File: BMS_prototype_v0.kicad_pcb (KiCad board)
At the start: 2 copper layers, 117 parts, among them J1 Conn_02x12_Odd_Even, J2 Conn_01x13_Pin, J3 Conn_01x02_Pin, J4 Conn_01x02_Pin, J5 Conn_02x08_Odd_Even, J7 Conn_01x03_Pin, Q2 Q_NMOS_GSD, Q3 Q_NMOS_GSD, Q4 Q_NMOS_GSD, Q5 Q_NMOS_GSD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

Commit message: add Res Shunt e atualiza para Kicad 9.0
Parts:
- removed NT1: NetTie_2, NetTie:NetTie-2_SMD_Pad0.5mm
- added SW1: SW_DIP_x01, Button_Switch_THT:SW_DIP_SPSTx01_Slide_6.7x4.1mm_W7.62mm_P2.54mm_LowProfile, F.Cu at (91.0, 74.2)
- Rsense1: footprint Resistor_SMD:R_0402_1005Metric -> footprints:S200_75
- moved C28 227.7 mm to (182.4, 86.2), turned to 90 degrees
- moved C27 227.1 mm to (182.4, 81.0), turned to 90 degrees
- moved R56 224.5 mm to (150.9, 119.0)
- moved C52 222.2 mm to (179.8, 92.9), turned to 180 degrees
- moved C46 220.4 mm to (163.3, 119.0)
- moved C51 201.9 mm to (157.4, 94.1), turned to 180 degrees
- moved C53 185.0 mm to (141.6, 94.7)
- moved Rsense1 61.6 mm to (86.1, 146.9), turned to 180 degrees
- moved R60 22.9 mm to (146.9, 94.9)
- moved J7 22.6 mm to (150.3, 104.9), turned to -90 degrees
- moved C47 13.6 mm to (124.0, 106.2), turned to 0 degrees
- moved R61 13.3 mm to (144.7, 119.0)
- moved R64 12.9 mm to (175.6, 110.4), turned to 90 degrees
- moved R63 11.5 mm to (172.6, 109.0)
- moved C48 10.8 mm to (124.0, 108.7), turned to 0 degrees
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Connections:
- J5 pad 1: unconnected-(J5-Pin_1-Pad1) -> EXTTS2
- J5 pad 10: RST_SHUT -> DFETOFF
- J5 pad 11: EXTTS2 -> REG1_3V3
- J5 pad 12: SDA -> DCHG
- J5 pad 13: REG1_3V3 -> GND
- J5 pad 14: SCL -> DDSG
- J5 pad 15: GND -> REG2
- J5 pad 16: REG2 -> RST_SHUT
- J5 pad 2: CFETOFF -> ALERT
- J5 pad 4: DFETOFF -> SCL
- J5 pad 6: DCHG -> SDA
- J5 pad 8: DDSG -> CFETOFF
- J5 pad 9: ALERT -> unconnected-(J5-Pin_9-Pad9)
- R64 pad 1: REG1_3V3 -> SCL
- R64 pad 2: SCL -> REG1_3V3
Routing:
- net PACK-: track 0.00 -> 133.6 mm
- net ALERT: track 0.00 -> 62.9 mm
- net CFETOFF: track 0.00 -> 60.2 mm
- net REG1_3V3: track 61.2 -> 121.1 mm, vias 0 -> 2
- net DFETOFF: track 0.00 -> 59.3 mm
- net SCL: track 3.50 -> 62.4 mm
- net DCHG: track 0.00 -> 58.4 mm
- net SDA: track 7.51 -> 62.2 mm
- net RST_SHUT: track 58.6 -> 108.9 mm
- net Net-(J7-Pin_3): track 0.00 -> 36.8 mm
- net EXTTS2: track 0.00 -> 36.5 mm
- net PACK+: track 70.2 -> 104.3 mm
- net BAT-: track 24.0 -> 49.4 mm
- net /Folha de monitoramento BMS/SRP: track 0.00 -> 21.0 mm
- net /Folha de monitoramento BMS/SRN: track 0.00 -> 19.1 mm
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- removed copper zone on F.Cu, net BAT-

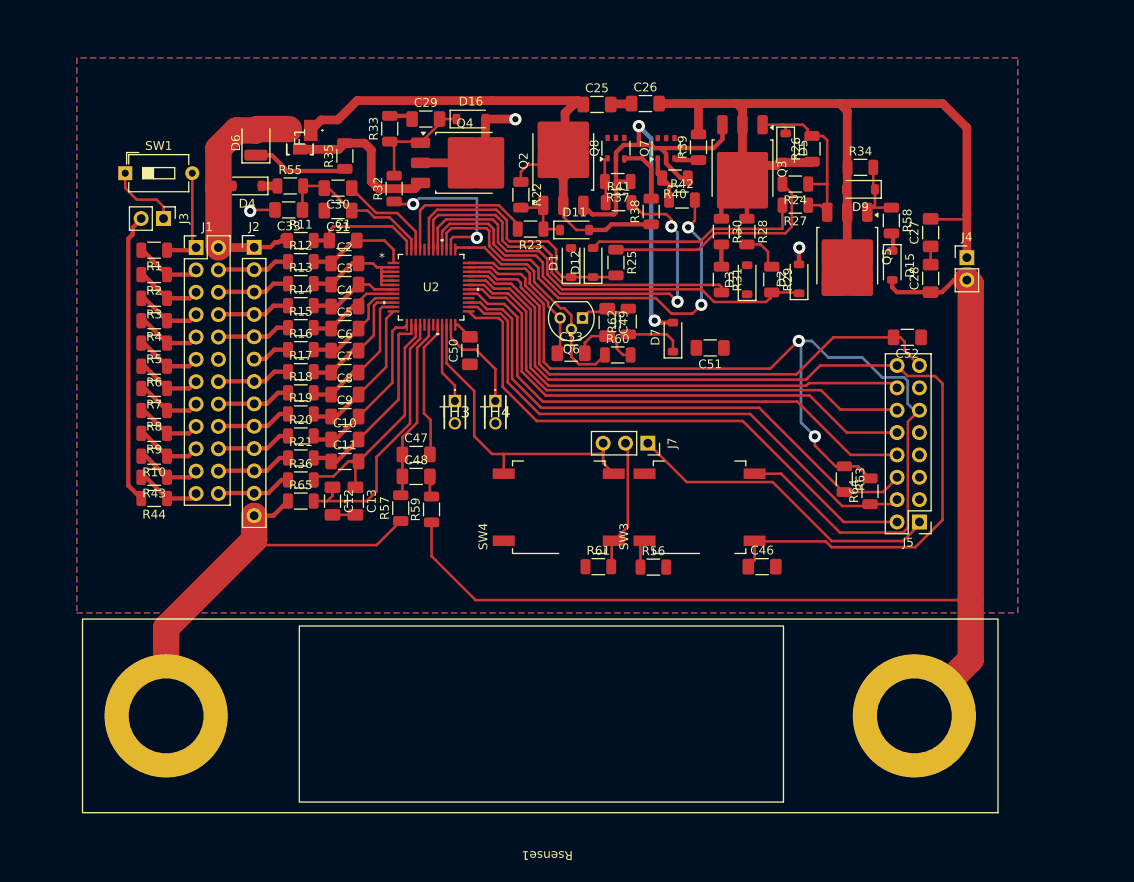
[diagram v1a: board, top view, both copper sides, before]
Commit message: Troca trilhas por regiões
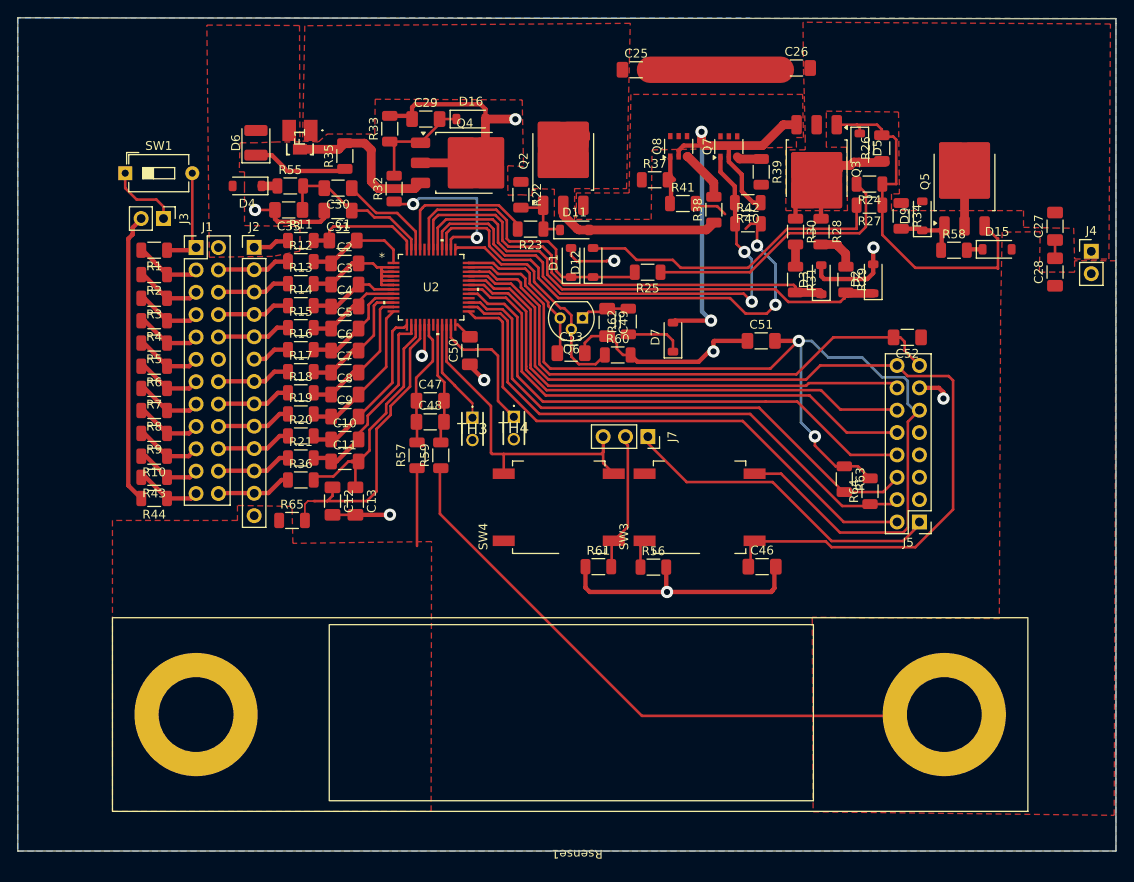
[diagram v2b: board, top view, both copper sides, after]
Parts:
- moved C26 17.6 mm to (167.2, 62.3)
- moved Q5 15.8 mm to (186.3, 75.2), turned to 90 degrees
- moved C27 14.1 mm to (196.6, 80.3)
- moved C28 14.1 mm to (196.6, 85.5)
- moved J4 14.1 mm to (200.7, 83.1)
- moved D15 12.1 mm to (190.0, 82.9), turned to 0 degrees
- moved R40 8.73 mm to (161.7, 77.6)
- moved D2 8.43 mm to (175.9, 86.2)
- moved D3 8.43 mm to (170.0, 86.3)
- moved D5 8.43 mm to (174.4, 71.4)
- moved Q3 8.43 mm to (169.5, 73.8)
- moved R24 8.43 mm to (175.5, 75.5)
- moved R27 8.43 mm to (175.5, 77.9)
- moved R28 8.43 mm to (170.0, 80.9)
- moved R29 8.42 mm to (172.8, 86.3)
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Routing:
- net GND: track 66.6 -> 158.1 mm, vias 3 -> 10
- net PACK+: track 104.3 -> 25.6 mm
- net PACK-: track 133.6 -> 72.6 mm
- net FBAT: track 61.4 -> 22.5 mm
- net BAT-: track 49.4 -> 13.6 mm
- net 12P: track 30.6 -> 4.18 mm
- net /Folha de proteção BMS/D_GATE: track 22.4 -> 41.1 mm
- net Net-(C25-Pad2): track 2.42 -> 14.9 mm
- net PACK: track 42.6 -> 54.0 mm
- net Net-(D12-A): track 25.1 -> 35.4 mm
- net LD: track 50.8 -> 59.4 mm
- net PCHG: track 49.7 -> 57.8 mm
- net CD: track 59.7 -> 51.6 mm
- net PDSG: track 50.0 -> 56.9 mm
- net /Folha de monitoramento BMS/SRP: track 21.0 -> 14.4 mm
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- added copper zone on F.Cu, net 12P
- added copper zone on F.Cu, net BAT-
- added copper zone on F.Cu, net CD
- added copper zone on F.Cu, net FBAT
- added copper zone on F.Cu, net PACK+
- added copper zone on F.Cu, net PACK-
- removed copper zone on F.Cu, net GND
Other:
- board outline added: 124.8 x 94.7 mm

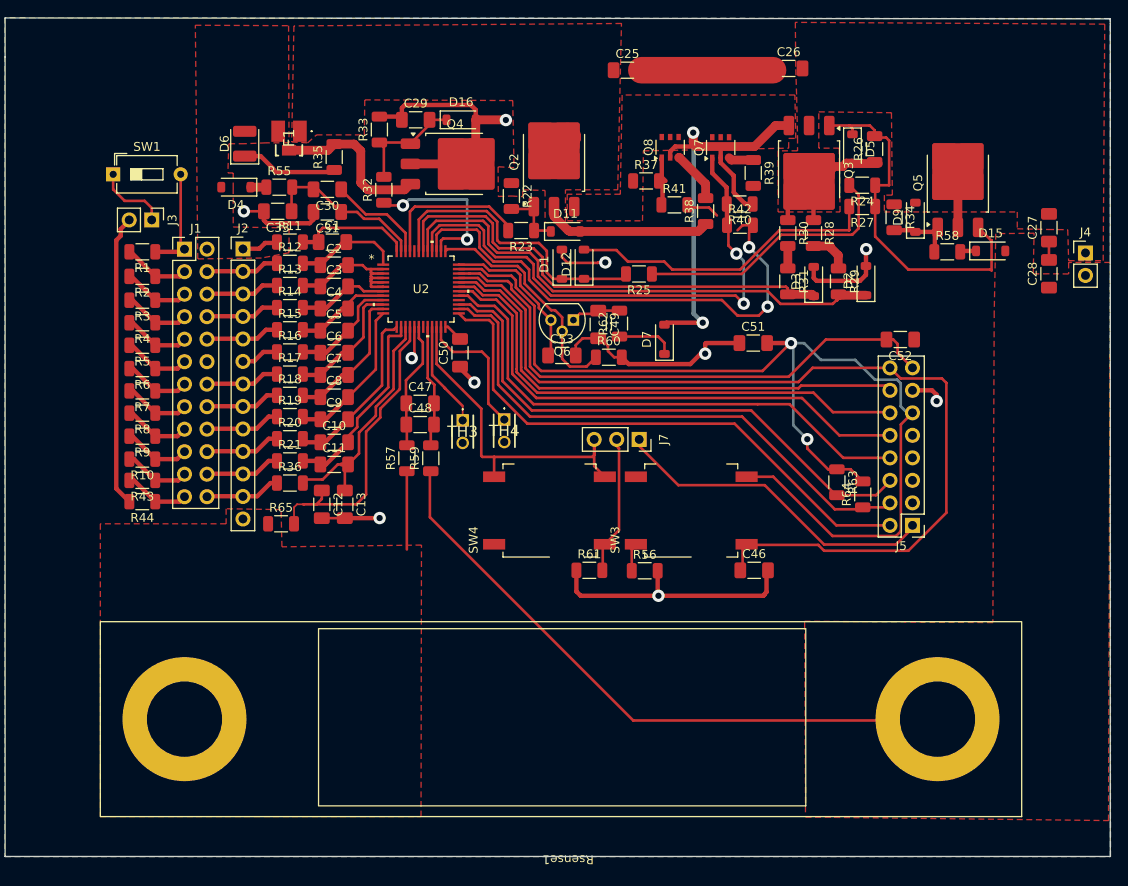
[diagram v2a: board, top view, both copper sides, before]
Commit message: Layout com footprints dos componentes da lista
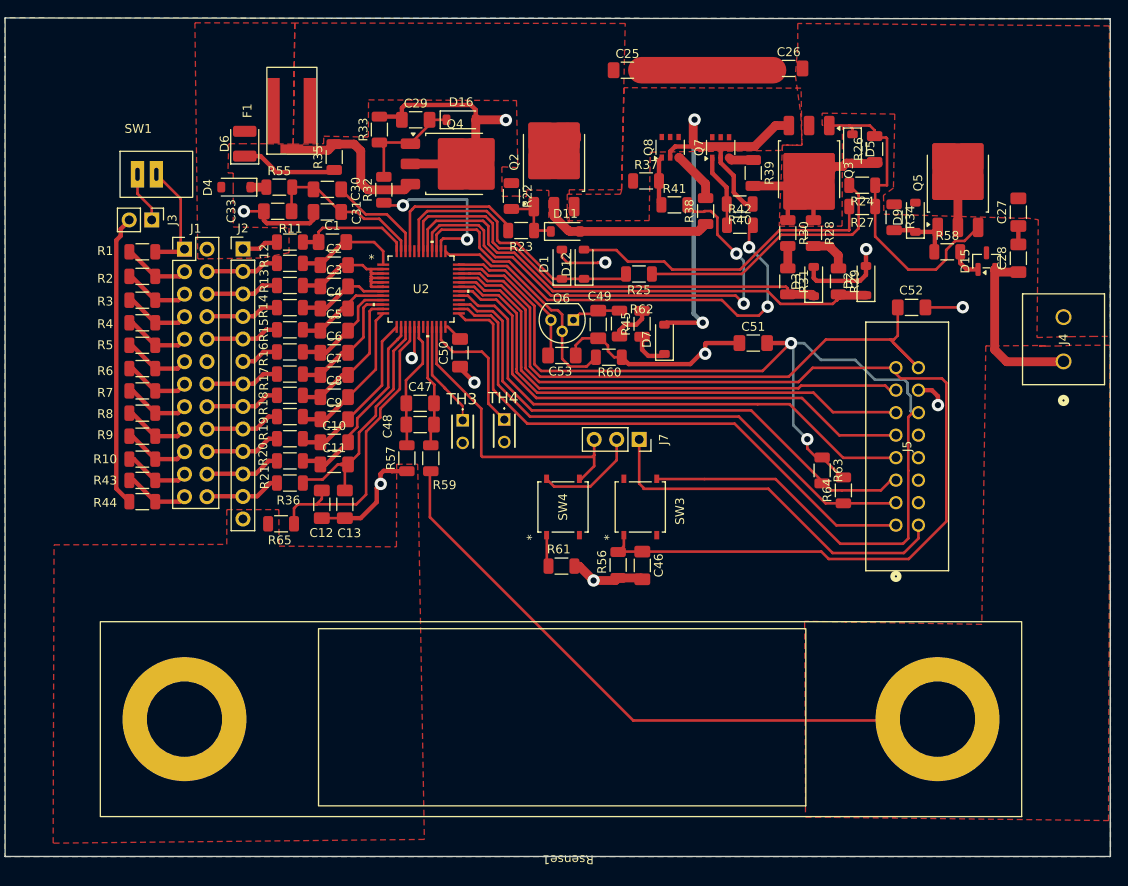
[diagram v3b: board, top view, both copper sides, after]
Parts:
- added NT1: NetTie_2, NetTie:NetTie-2_SMD_Pad0.5mm, F.Cu at (122.0, 107.7)
- added R45: 220, Resistor_SMD:R_1206_3216Metric, F.Cu at (150.7, 91.1)
- D15: footprint Diode_SMD:D_SOD-123 -> Package_TO_SOT_SMD:SOT-23
- F1: value ITV4030L1412NR -> SCF9550; footprint footprints:ITV4030L1412NR -> SCF-9550:Sem título
- J4: footprint Connector_PinHeader_2.54mm:PinHeader_1x02_P2.54mm_Vertical -> footprints:CONN_1935776_PXC
- J5: footprint Connector_PinHeader_2.54mm:PinHeader_2x08_P2.54mm_Vertical -> footprints:CONN16_SBH11-PBPC-D08-ST-BK_SUL
- R11, R12, R13, R14, R15, R16, R17, R18, R19, R20, R21, R36, R63, R64, R65: value R -> 20
- R38, R39: value 1k -> 2k
- SW1: footprint Button_Switch_THT:SW_DIP_SPSTx01_Slide_6.7x4.1mm_W7.62mm_P2.54mm_LowProfile -> footprints:SWT31AAA3S1
- SW3, SW4: footprint Button_Switch_SMD:SW_MEC_5GSH9 -> footprints:SMT_FS
- moved C46 12.6 mm to (150.7, 118.4), turned to -90 degrees
- moved J4 12.5 mm to (198.2, 95.4), turned to 90 degrees
- moved SW3 5.76 mm to (150.4, 111.8)
- moved C28 3.88 mm to (193.1, 83.7)
- moved C27 3.88 mm to (193.1, 78.5)
- moved C52 3.84 mm to (181.1, 89.3)
- moved R61 3.19 mm to (141.6, 118.5), turned to 180 degrees
- moved F1 3.08 mm to (111.1, 67.1)
- moved R56 3.07 mm to (147.9, 118.3), turned to -90 degrees
- moved SW1 2.74 mm to (93.7, 74.2)
- moved R64 2.23 mm to (173.4, 109.9)
- moved R63 2.13 mm to (171.0, 107.7)
- moved J5 1.87 mm to (179.3, 113.9), turned to 90 degrees
- moved SW4 1.58 mm to (141.7, 111.8)
- moved D15 1.24 mm to (189.5, 84.0), turned to 90 degrees
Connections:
- F1 pad 1: FBAT -> 12P
- F1 pad 3: 12P -> FBAT
- J4 pad 1: PACK+ -> PACK-
- J4 pad 2: PACK- -> PACK+
- J5 pad 1: EXTTS2 -> ALERT
- J5 pad 10: DFETOFF -> unconnected-(J5-Pin_10-Pad10)
- J5 pad 11: REG1_3V3 -> DCHG
- J5 pad 12: DCHG -> REG1_3V3
- J5 pad 13: GND -> DDSG
- J5 pad 14: DDSG -> GND
- J5 pad 15: REG2 -> RST_SHUT
- J5 pad 16: RST_SHUT -> REG2
- J5 pad 2: ALERT -> EXTTS2
- J5 pad 3: unconnected-(J5-Pin_3-Pad3) -> SCL
- J5 pad 4: SCL -> unconnected-(J5-Pin_4-Pad4)
- J5 pad 5: unconnected-(J5-Pin_5-Pad5) -> SDA
- J5 pad 6: SDA -> unconnected-(J5-Pin_6-Pad6)
- J5 pad 7: unconnected-(J5-Pin_7-Pad7) -> CFETOFF
- J5 pad 8: CFETOFF -> unconnected-(J5-Pin_8-Pad8)
- J5 pad 9: unconnected-(J5-Pin_9-Pad9) -> DFETOFF
- R62 pad 1: Net-(D7-K) -> Net-(R45-Pad2)
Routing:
- net PACK-: track 72.6 -> 92.9 mm
- net GND: track 158.1 -> 146.0 mm, vias 10 -> 11
- net RST_SHUT: track 110.9 -> 122.1 mm
- net REG1_3V3: track 123.9 -> 133.4 mm
- net REG2: track 63.9 -> 71.9 mm
- net BAT-: track 13.6 -> 6.67 mm
- net EXTTS2: track 36.5 -> 42.0 mm
- net PACK+: track 25.6 -> 30.8 mm
- net /Folha de proteção BMS/D_GATE: track 41.1 -> 36.2 mm
- net Net-(R45-Pad2): track 0.00 -> 4.08 mm
- net CD: track 51.6 -> 54.7 mm
- net PDSG: track 56.9 -> 54.2 mm
- net /DC_48V: track 8.27 -> 5.81 mm
- net Net-(D7-K): track 6.62 -> 4.51 mm
- net Net-(J7-Pin_3): track 36.8 -> 34.8 mm
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
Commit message: layout final de componentes, com footprints da lista de componentes mais uma adição de via GND
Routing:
- net GND: track 146.0 -> 116.0 mm, vias 11 -> 12
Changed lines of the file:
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@@
-	)
-	(segment
-		(start 91.8 81.2)
-		(end 91.8 80.435)
-		(width 0.5)
-		(layer "F.Cu")
-		(net 92)
 	)
 	(segment
@@
 	)
 	(segment
-		(start 91.8 80.435)
-		(end 92.835 79.4)
-		(width 0.5)
-		(layer "F.Cu")
-		(net 92)
-	)
-	(segment
 		(start 131.875 66.975)
 		(end 131.875 68.1)
@@
 	)
 	(segment
+		(start 92.775 111.2)
+		(end 92.775 114.225)
+		(width 0.5)
+		(layer "F.Cu")
+		(net 92)
+	)
+	(segment
 		(start 145.9625 92.7625)
 		(end 146.8 93.6)
@@
 	)
 	(segment
-		(start 91.3 109.725)
-		(end 92.775 111.2)
-		(width 0.5)
-		(layer "F.Cu")
-		(net 92)
-	)
-	(segment
 		(start 135.25 68.1)
 		(end 135.275 68.125)
@@
 	)
 	(segment
-		(start 91.3 81.7)
-		(end 91.3 109.725)
-		(width 0.5)
-		(layer "F.Cu")
-		(net 92)
-	)
-	(segment
 		(start 175.925 85.6)
 		(end 175.925 84.6)
@@
 	)
 	(segment
-		(start 91.8 81.2)
-		(end 91.3 81.7)
-		(width 0.5)
-		(layer "F.Cu")
-		(net 92)
-	)
-	(segment
 		(start 157.775 94.5)
 		(end 157.775 93.4)
@@
 		(size 1.4)
 		(drill 0.7)
+		(layers "F.Cu" "B.Cu")
+		(net 92)
+	)
+	(via
+		(at 92.775 114.225)
+		(size 1.4)
+		(drill 0.7)
